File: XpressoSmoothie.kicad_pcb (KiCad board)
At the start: 2 copper layers, 99.7 x 99.7 mm, 130 parts, among them J1 HEADER_4, J10 HEADER_3X2, J11 Pwr_in, J12 HEADER_4, J13 HEADER_4X2, J14 HEADER_3X2, J15 HEADER_4, J16 HEADER_4, J17 HEADER_4, J172 HEADER_2, J18 HEADER_4, J19 HEADER_2, J2 HEADER_4, J20 HEADER_2, J21 HEADER_2, J22 HEADER_2, J23 HEADER_4, J232 HEADER_2, J24 HEADER_4, J25 HEADER_4, J252 HEADER_2, J26 USB, J27 HEADER_4, J28 MICROSD-MOLEX, J3 HEADER_3, J4 HEADER_3X2, J5 HEADER_3X2, J6 LPCXPRESSO_GENERIC_HEADER, J7 HEADER_4, J8 HEADER_4, J9 HEADER_3X2, M1 LOGO_OSHW, M2 LOGO_OSHW, Q1 IRLB 8743, Q2 IRLB 8743, Q3 IRLB 8743, Q4 IRLB 8743, SW1 SW_PUSH, SW2 SW_PUSH, U1 POLOLU_A4988, U10 TC4422A, U11 TC4422A, U12 LM1117-3.3, U2 POLOLU_A4988, U3 POLOLU_A4988, U4 POLOLU_A4988, U5 POLOLU_A4988, U7 LM7809CT, U8 TC4422A, U9 TC4422A

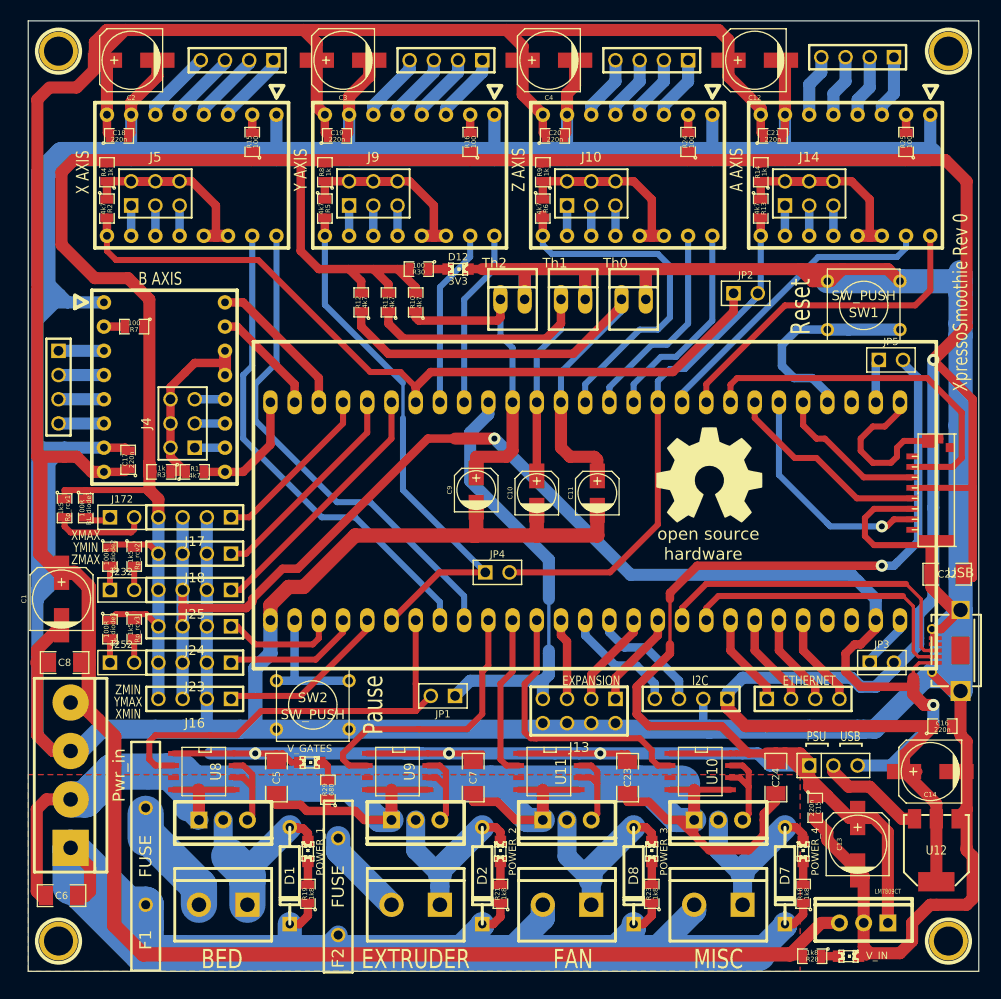
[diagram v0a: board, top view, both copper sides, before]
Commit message: Reset to using SD detect.
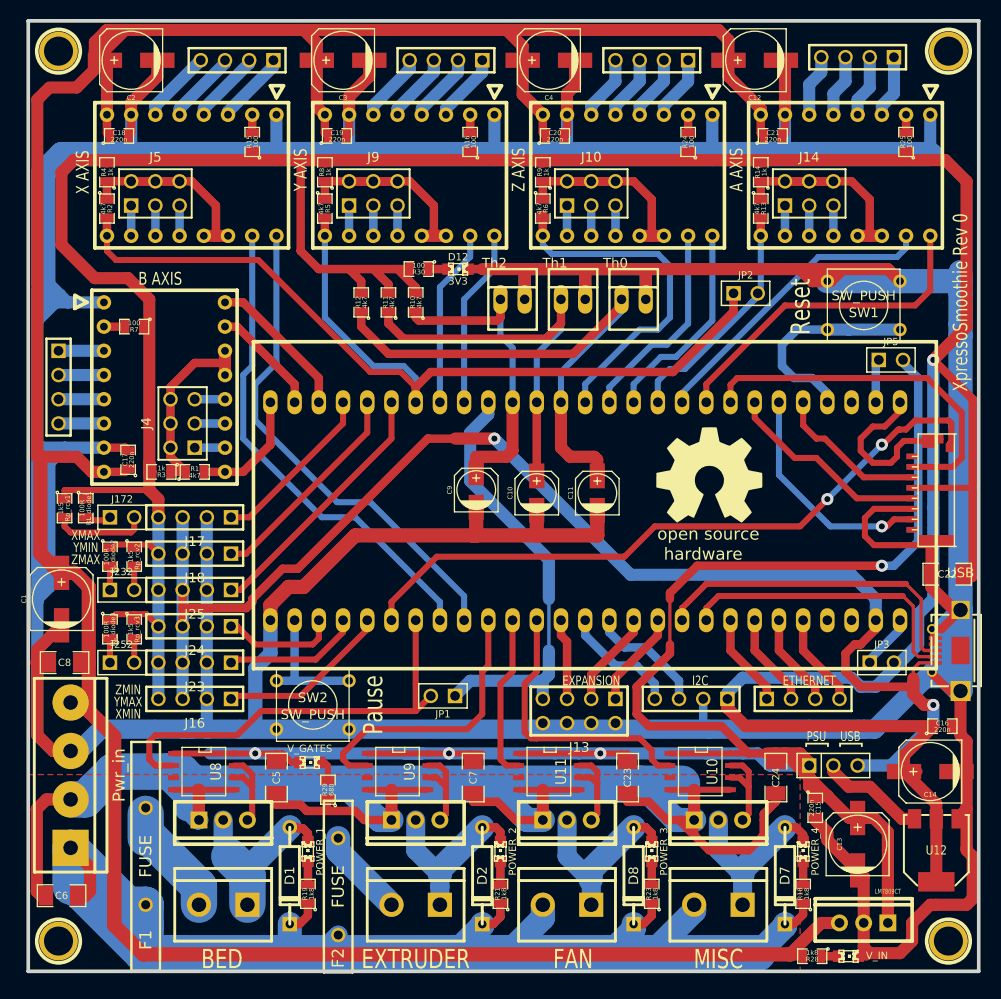
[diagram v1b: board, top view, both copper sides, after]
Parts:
- removed JP4: JUMPER-2, PIN_ARRAY_2X1
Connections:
- J28 pad DET: N-0000085 -> SD_card_detect
- J6 pad 49: Y-EN -> SD_card_detect
- R5 pad 2: Y-EN -> X-EN
- U3 pad 9: Y-EN -> X-EN
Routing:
- net SD_card_detect: track 0.00 -> 71.3 mm, vias 0 -> 2
- net Y-EN: track 56.1 -> 0.00 mm
- net A-EN: track 56.4 -> 26.0 mm
- net X-EN: track 83.5 -> 108.7 mm

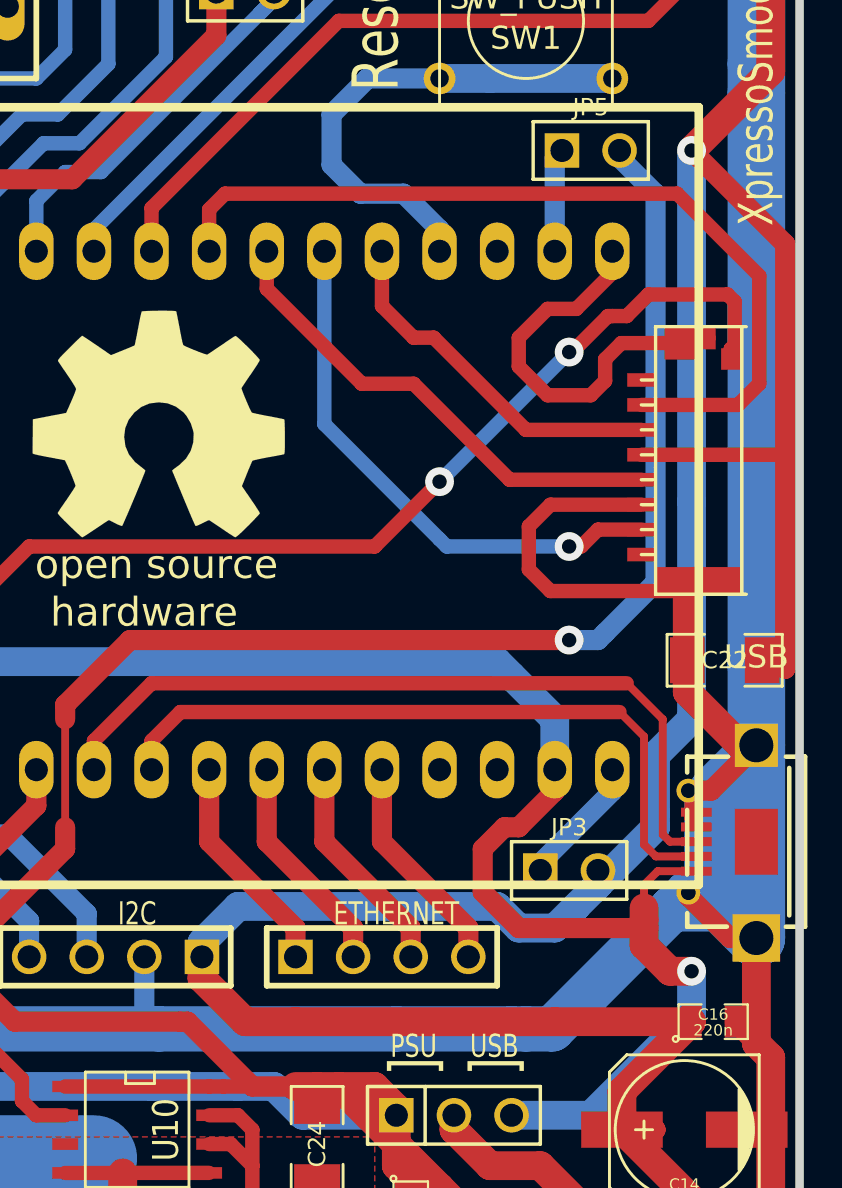
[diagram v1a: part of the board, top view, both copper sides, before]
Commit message: Reverted back to using SD detect. Added jumper to connect/disconnect 5V line to USB Vbus. I think this finally means we're compatible with the mbed, so closing #11 again.
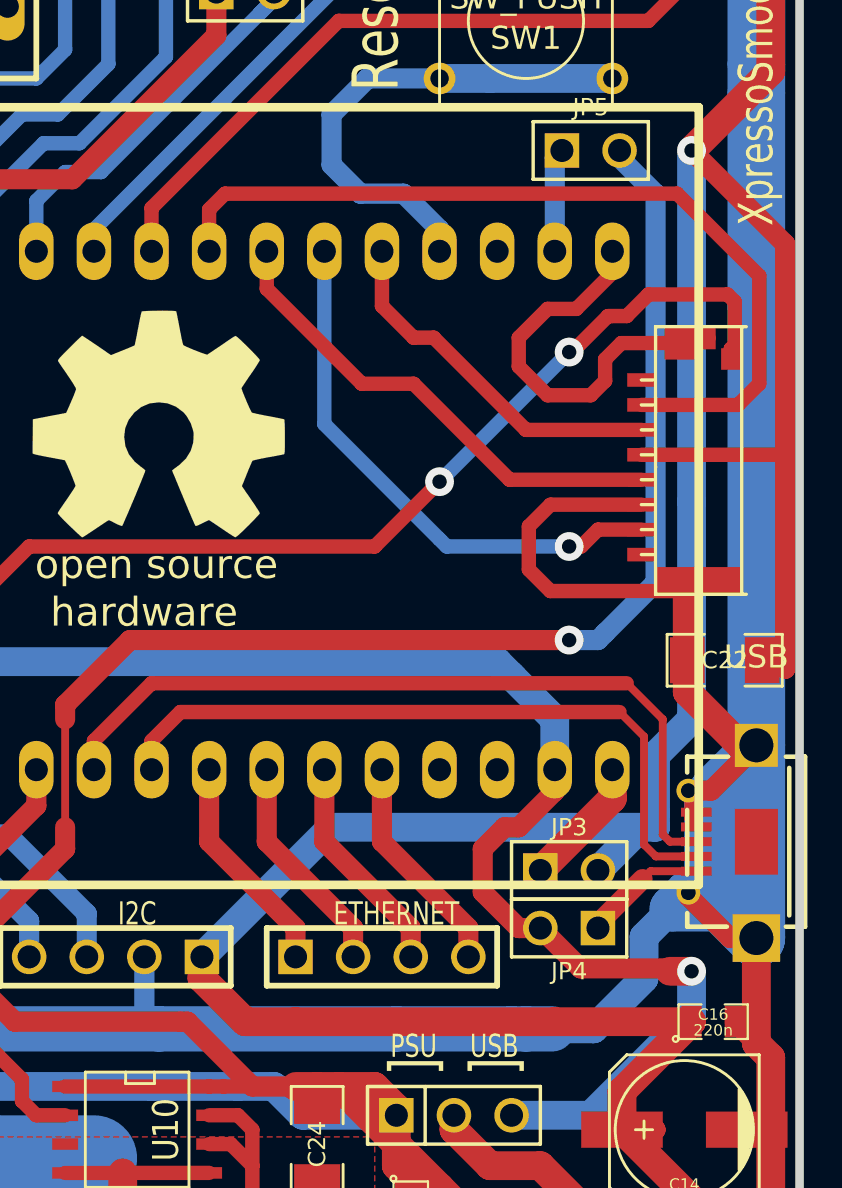
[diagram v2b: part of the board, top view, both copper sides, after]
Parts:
- added JP4: JUMPER-2, PIN_ARRAY_2X1, F.Cu at (161.3, 123.8)
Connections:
- J26 pad 1: +5V -> N-0000014
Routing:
- net N-0000014: track 0.00 -> 5.49 mm
- net +5V: track 146.6 -> 141.7 mm
- net GND: track 761.0 -> 762.1 mm

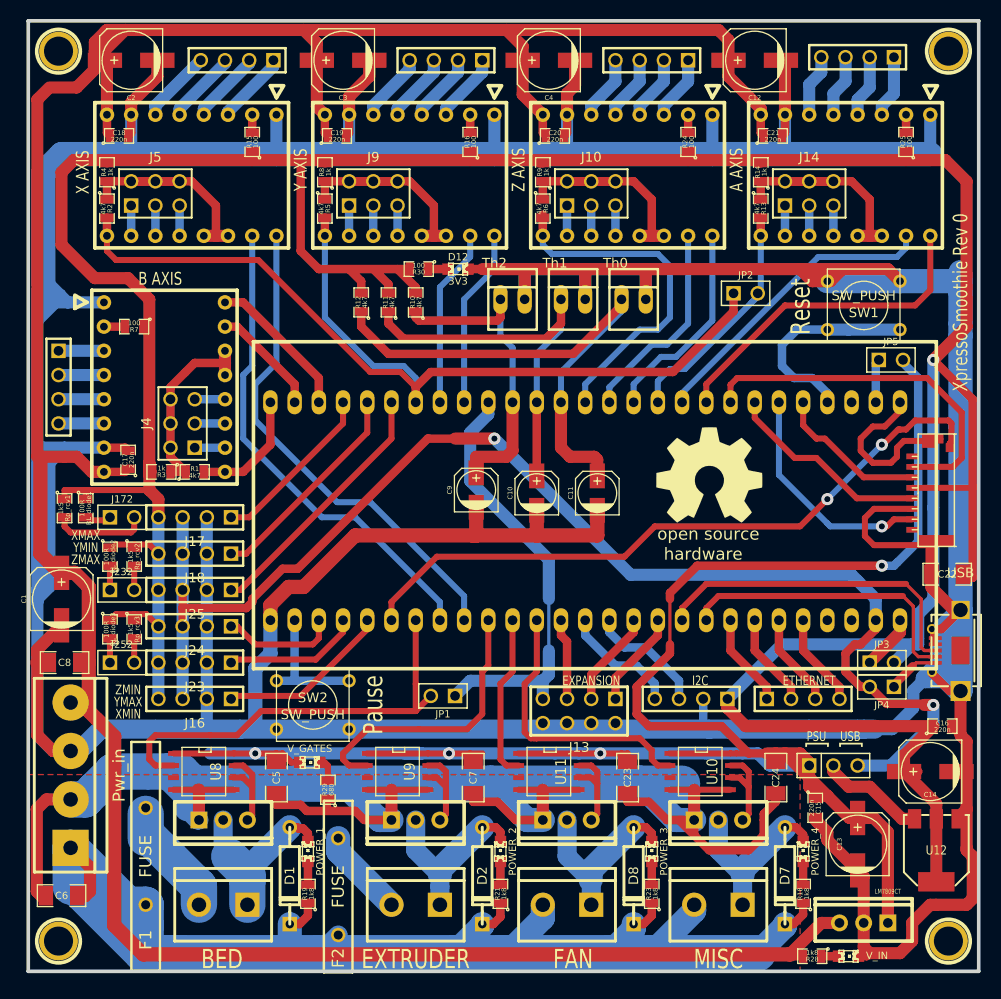
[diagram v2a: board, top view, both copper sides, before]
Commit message: Fixed up fuses (which were hanging slightly over the edge) and thinned edge graphics for clarity.
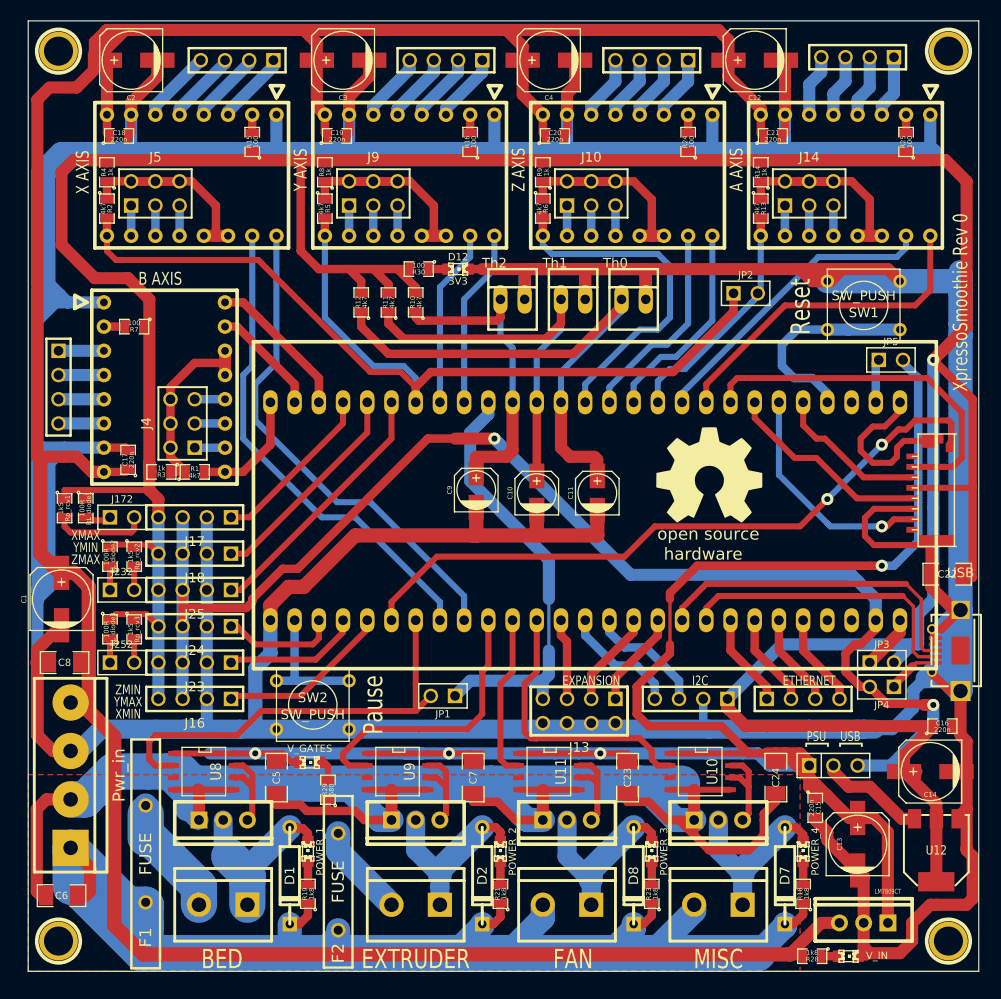
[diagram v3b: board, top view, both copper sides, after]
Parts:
- moved F2 0.51 mm to (104.3, 144.3)
- moved F1 0.25 mm to (84.1, 141.4)
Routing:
- net N-0000052: track 12.3 -> 15.7 mm
- net N-0000053: track 9.30 -> 9.81 mm
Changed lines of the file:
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@@
     (links 344)
     (no_connects 11)
-    (area 71.564499 53.784499 171.640501 153.860501)
+    (area 56.388 52.51262 179.864657 163.2712)
     (thickness 1.6)
     (drawings 31)
-    (tracks 1190)
+    (tracks 1194)
     (zones 0)
     (modules 130)
@@
   )
   (setup
-    (last_trace_width 1.27)
+    (last_trace_width 2.54)
     (user_trace_width 0.35)
     (user_trace_width 0.889)
@@
     (trace_min 0.35)
     (segment_width 0.381)
-    (edge_width 0.381)
+    (edge_width 0.0254)
     (via_size 1.27)
     (via_drill 0.635)
@@
   )
   (module MF-R500 (layer F.Cu)
-    (at 104.267 144.78 90)
+    (at 104.267 144.272 90)
     (fp_text reference F2 (at -7.493 0 90) (layer F.SilkS)
       (effects (font (thickness 0.3048)))
@@
   )
   (module MF-R1100 (layer F.Cu)
-    (at 84.074 141.605 90)
+    (at 84.074 141.351 90)
     (fp_text reference F1 (at -8.763 0 90) (layer F.SilkS)
       (effects (font (thickness 0.3048)))
@@
     (effects (font (size 1.524 1.143) (thickness 0.2286)))
   )
-  (gr_line (start 71.755 53.975) (end 71.755 153.67) (angle 90) (layer Edge.Cuts) (width 0.381))
-  (gr_line (start 171.45 53.975) (end 71.755 53.975) (angle 90) (layer Edge.Cuts) (width 0.381))
-  (gr_line (start 171.45 153.67) (end 171.45 53.975) (angle 90) (layer Edge.Cuts) (width 0.381))
-  (gr_line (start 71.755 153.67) (end 171.45 153.67) (angle 90) (layer Edge.Cuts) (width 0.381))
+  (gr_line (start 71.755 53.975) (end 71.755 153.67) (angle 90) (layer Edge.Cuts) (width 0.0254))
+  (gr_line (start 171.45 53.975) (end 71.755 53.975) (angle 90) (layer Edge.Cuts) (width 0.0254))
+  (gr_line (start 171.45 153.67) (end 171.45 53.975) (angle 90) (layer Edge.Cuts) (width 0.0254))
+  (gr_line (start 71.755 153.67) (end 171.45 153.67) (angle 90) (layer Edge.Cuts) (width 0.0254))
   (dimension 99.695 (width 0.3048) (layer Cmts.User)
     (gr_text "99.695 mm" (at 121.6025 161.645599) (layer Cmts.User)
@@
   (segment (start 165.1 132.715) (end 163.61918 132.715) (width 0.889) (layer F.Cu) (net 1))
   (segment (start 167.005 144.272) (end 167.005 137.668) (width 1.27) (layer F.Cu) (net 1))
-  (segment (start 160.02 123.825) (end 161.798 125.603) (width 0.889) (layer F.Cu) (net 2) (status 400000))
+  (segment (start 160.02 123.825) (end 161.798 125.603) (width 0.889) (layer F.Cu) (net 2))
   (segment (start 165.735 125.73) (end 166.6875 125.73) (width 1.27) (layer F.Cu) (net 2))
   (via (at 166.6875 125.73) (size 1.27) (layers F.Cu B.Cu) (net 2))
@@
   (segment (start 165.608 125.603) (end 165.735 125.73) (width 0.889) (layer F.Cu) (net 2))
   (segment (start 161.798 125.603) (end 165.608 125.603) (width 0.889) (layer F.Cu) (net 2))
-  (segment (start 160.02 123.825) (end 159.0675 123.825) (width 0.889) (layer F.Cu) (net 2) (status 400000))
+  (segment (start 160.02 123.825) (end 159.0675 123.825) (width 0.889) (layer F.Cu) (net 2))
   (segment (start 158.4325 119.38) (end 157.48 120.3325) (width 0.889) (layer F.Cu) (net 2))
   (segment (start 157.48 120.3325) (end 157.48 122.2375) (width 0.889) (layer F.Cu) (net 2))
@@
   (segment (start 86.6775 99.695) (end 86.6775 98.7425) (width 0.889) (layer F.Cu) (net 39))
   (segment (start 86.6775 93.6625) (end 86.6775 98.7425) (width 0.889) (layer F.Cu) (net 39))
-  (segment (start 166.89578 121.31548) (end 164.87902 121.31548) (width 0.35) (layer F.Cu) (net 52) (status 400000))
-  (segment (start 162.56 123.6345) (end 164.5285 121.666) (width 0.889) (layer F.Cu) (net 52) (status 400000))
-  (segment (start 162.56 123.6345) (end 162.56 123.825) (width 0.889) (layer F.Cu) (net 52) (status C00000))
+  (segment (start 166.89578 121.31548) (end 164.87902 121.31548) (width 0.35) (layer F.Cu) (net 52))
+  (segment (start 162.56 123.6345) (end 164.5285 121.666) (width 0.889) (layer F.Cu) (net 52))
+  (segment (start 162.56 123.6345) (end 162.56 123.825) (width 0.889) (layer F.Cu) (net 52))
   (segment (start 164.87902 121.31548) (end 164.5285 121.666) (width 0.35) (layer F.Cu) (net 52))
   (segment (start 153.67 70.8025) (end 151.13 70.8025) (width 0.889) (layer F.Cu) (net 53))
@@
   (segment (start 157.7975 134.3025) (end 160.02 134.3025) (width 1.27) (layer F.Cu) (net 79))
   (segment (start 156.21 132.715) (end 157.7975 134.3025) (width 1.27) (layer F.Cu) (net 79))
-  (segment (start 84.074 137.16) (end 84.074 136.525) (width 2.54) (layer B.Cu) (net 80))
+  (segment (start 84.074 136.271) (end 84.074 139.7) (width 2.54) (layer B.Cu) (net 80) (status 400000))
   (segment (start 84.074 139.7) (end 84.074 137.16) (width 3.81) (layer B.Cu) (net 80))
+  (segment (start 84.074 137.16) (end 84.074 136.525) (width 2.54) (layer B.Cu) (net 80))
   (segment (start 89.662 144.78) (end 84.582 139.7) (width 3.81) (layer B.Cu) (net 80))
   (segment (start 89.662 146.685) (end 89.662 144.78) (width 3.81) (layer B.Cu) (net 80))
+  (segment (start 104.267 139.192) (end 104.267 139.7) (width 2.54) (layer B.Cu) (net 81))
   (segment (start 104.267 139.7) (end 104.267 141.097) (width 2.54) (layer B.Cu) (net 81))
   (segment (start 104.267 141.097) (end 109.855 146.685) (width 2.54) (layer B.Cu) (net 81))
@@
   (segment (start 113.03 130.81) (end 111.125 130.81) (width 1.27) (layer B.Cu) (net 122))
   (segment (start 84.074 146.685) (end 82.169 146.685) (width 3.81) (layer B.Cu) (net 123))
+  (segment (start 84.074 146.685) (end 84.074 148.844) (width 3.81) (layer B.Cu) (net 123))
   (segment (start 82.169 146.685) (end 76.2 140.716) (width 3.81) (layer B.Cu) (net 123))
+  (segment (start 104.267 149.352) (end 104.267 149.9235) (width 2.54) (layer B.Cu) (net 123))
+  (segment (start 104.267 149.9235) (end 102.4255 151.765) (width 2.54) (layer B.Cu) (net 123))
   (segment (start 76.2 140.716) (end 76.2 140.97) (width 3.81) (layer B.Cu) (net 123))
   (segment (start 76.2 140.97) (end 84.074 148.844) (width 3.81) (layer B.Cu) (net 123))
@@
   (segment (start 116.459 151.765) (end 121.285 151.765) (width 3.81) (layer B.Cu) (net 123))
   (segment (start 122.047 151.765) (end 132.715 151.765) (width 3.81) (layer B.Cu) (net 123))
-  (segment (start 102.235 151.765) (end 116.459 151.765) (width 3.81) (layer B.Cu) (net 123))
+  (segment (start 102.235 151.765) (end 102.4255 151.765) (width 3.81) (layer B.Cu) (net 123))
+  (segment (start 102.4255 151.765) (end 116.459 151.765) (width 3.81) (layer B.Cu) (net 123))
   (segment (start 132.715 151.765) (end 137.16 151.765) (width 3.81) (layer B.Cu) (net 123))
   (segment (start 137.16 151.765) (end 148.2725 151.765) (width 3.81) (layer B.Cu) (net 123))
-  (segment (start 104.267 149.86) (end 102.362 151.765) (width 2) (layer B.Cu) (net 123))
   (segment (start 99.568 151.765) (end 101.727 151.765) (width 3.81) (layer B.Cu) (net 123))
   (segment (start 102.362 151.765) (end 101.727 151.765) (width 2) (layer B.Cu) (net 123))
   (segment (start 97.917 151.765) (end 99.568 151.765) (width 3.81) (layer B.Cu) (net 123))
-  (segment (start 84.074 146.685) (end 84.074 148.844) (width 3.81) (layer B.Cu) (net 123))
   (segment (start 84.074 148.844) (end 84.074 151.765) (width 3.81) (layer B.Cu) (net 123))
   (segment (start 84.074 151.765) (end 84.074 151.765) (width 3.81) (layer B.Cu) (net 123))
